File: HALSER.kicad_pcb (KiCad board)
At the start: 4 copper layers, 90.8 x 58.8 mm, 187 parts, among them J1001 RX Sel Header, J1002 RS485 RX Socket, J1003 RS485 TX Socket, J1004 RS-232 Socket, J1005 UART Socket, J301 GPIO, J401 I2C Female Header, J402 I2C Male Header, J501 1-Wire Male Header, J701 CAN Socket, J702 Vin header, J703 CAN Header, J802 USB_C_Receptacle_USB2.0_16P, SW301 SW_Push, SW302 SW_Push, U1001 SN75176BDR, U1002 74LVC2G17, U1003 SP3232EEY-L/TR, U1004 SN75176BDR, U201 SN65HVD230DR, U301 ESP32-C3-MINI-1, U701 LMR54410DBVR, U901 π122U31, U902 XC6206P332MR

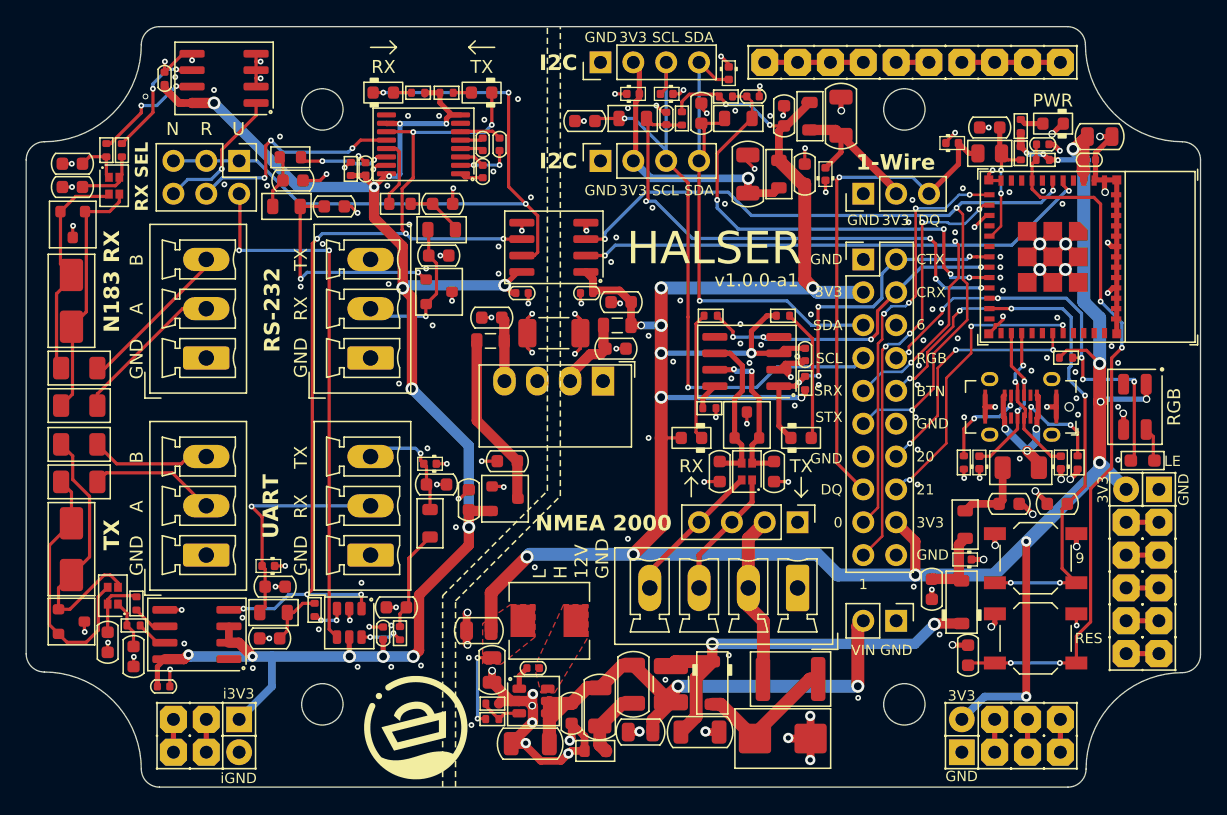
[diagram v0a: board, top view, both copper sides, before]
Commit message: Fix issues found in -a1
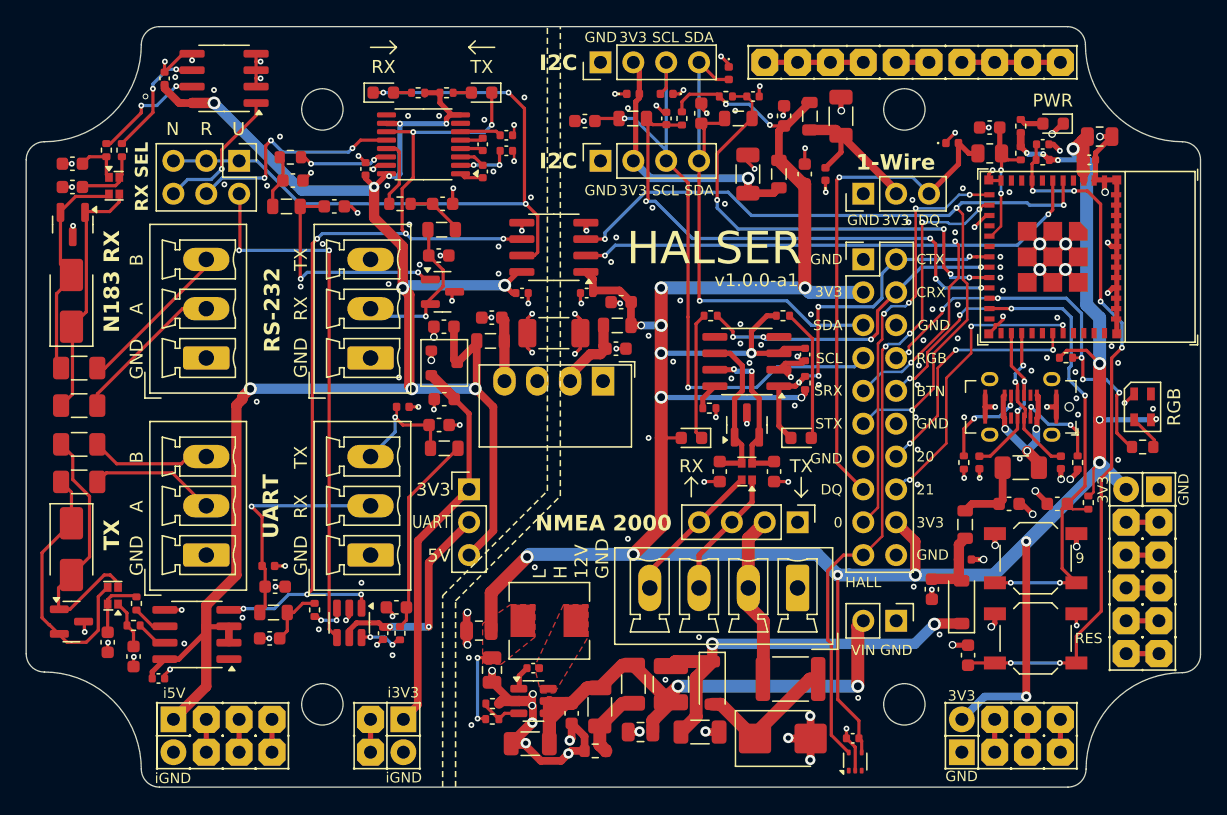
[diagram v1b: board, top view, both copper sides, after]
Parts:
- removed G606: HL-Pictogram, HALSER:HaL_picto_8mm
- removed R901: 330R, PCM_Resistor_SMD_AKL:R_0402_1005Metric
- added C1020: 100nF, Capacitor_SMD:C_0402_1005Metric, F.Cu at (125.7, 85.0)
- added C306: 100nF, Capacitor_SMD:C_0402_1005Metric, F.Cu at (152.5, 131.6)
- added JP1001: UART V-sel, Connector_PinHeader_2.54mm:PinHeader_1x03_P2.54mm_Vertical, F.Cu at (122.8, 112.4)
- added R307: 10k, Resistor_SMD:R_0402_1005Metric, F.Cu at (170.7, 113.4)
- added REF**: ProtoPad_1x01_P2.54_D2.0, HALSER:ProtoPad_1x01_P2.54_D2.0, F.Cu at (117.8, 132.7)
- added REF**: ProtoPad_1x02_P2.54_2.1x2.1_Octagonal, HALSER:ProtoPad_1x02_P2.54_2.1x2.1_Octagonal, F.Cu at (107.6, 132.7)
- added REF**: ProtoPad_1x02_P2.54_2.1x2.1_Octagonal, HALSER:ProtoPad_1x02_P2.54_2.1x2.1_Octagonal, F.Cu at (115.2, 132.7)
- added REF**: ProtoPad_1x01_P2.54_2.0x2.0, HALSER:ProtoPad_1x01_P2.54_2.0x2.0, F.Cu at (117.8, 130.2)
- added U302: KTH1601TL-SF5, Package_TO_SOT_SMD:SOT-553, F.Cu at (152.7, 133.4)
- C1001, C1002, C1003, C1004, C1005, C1006, C1007, C203, C303, C305, C405, C406, C707, C902, C906: footprint PCM_Capacitor_SMD_AKL:C_0402_1005Metric -> Capacitor_SMD:C_0402_1005Metric
- C1008, C1009, C1010, C1011, C1012, C1013, C1014, C1015, C1016, C1017, C1018, C1019, C201, C202, C301, C302, C402, C403, C404, C502, C503, C706, C801, C802, C901, C903, C905, C907, C908: footprint PCM_Capacitor_SMD_AKL:C_0603_1608Metric -> Capacitor_SMD:C_0603_1608Metric
- C304, C702, C708, C709: footprint PCM_Capacitor_SMD_AKL:C_0805_2012Metric -> Capacitor_SMD:C_0805_2012Metric
- C401, C501, C701, C703, C704, C705: footprint PCM_Capacitor_SMD_AKL:C_1206_3216Metric -> Capacitor_SMD:C_1206_3216Metric
- D1001, D1002, D301, D302, D303: footprint PCM_LED_SMD_AKL:LED_0603_1608Metric -> LED_SMD:LED_0603_1608Metric
- D1003, D1004, D1008, D201: footprint PCM_Package_TO_SOT_SMD_AKL:SOT-23 -> Package_TO_SOT_SMD:SOT-23
- D1005, D1006: footprint PCM_Diode_SMD_AKL:D_SMA_TVS -> Diode_SMD:D_SMA
- D1007, D1009, D401, D402, D403, D501, D502, D801, D802, D803: footprint PCM_Diode_SMD_AKL:D_0402_1005Metric -> Diode_SMD:D_0402_1005Metric
- D701, D703: footprint PCM_Diode_SMD_AKL:D_SOD-123 -> Diode_SMD:D_SOD-123
- D702: footprint PCM_Diode_SMD_AKL:D_SMB_TVS -> Diode_SMD:D_SMB
- F1001, F1002, F1003, F1004, F801: footprint PCM_Fuse_AKL:Fuse_1206_3216Metric -> Fuse:Fuse_1206_3216Metric
- F701: footprint PCM_Fuse_AKL:Fuse_1812_4532Metric -> Fuse:Fuse_1812_4532Metric
- FB1001, FB1002, FB1003, FB1004, FB401, FB402, FB403, FB501, FB801: footprint PCM_Ferrite_SMD_AKL:Ferrite_0805_2012Metric -> Inductor_SMD:L_0805_2012Metric
- LED301: value SK68XX-MINI-HS -> SK6805-MICRO-J; footprint PCM_LED_SMD_AKL:LED_SK6812MINI_PLCC4_3.5x3.5mm_P1.75mm -> HALSER:LED_SK6805_PLCC4_2.4x2.7mm_P1.3mm
- R1001, R1002: value 1.5k -> 2.2k; footprint PCM_Resistor_SMD_AKL:R_0402_1005Metric -> Resistor_SMD:R_0402_1005Metric
- R1003, R1004, R1005, R1006, R1007, R1008, R203, R204, R301, R302, R303, R304, R305, R401, R402, R501, R702, R703, R801, R802: footprint PCM_Resistor_SMD_AKL:R_0402_1005Metric -> Resistor_SMD:R_0402_1005Metric
- R1009, R1010, R701: footprint PCM_Resistor_SMD_AKL:R_0603_1608Metric -> Resistor_SMD:R_0603_1608Metric
- R306: value 0R -> 470R; footprint PCM_Resistor_SMD_AKL:R_0603_1608Metric_Pad0.98x0.95mm_HandSolder -> Resistor_SMD:R_0603_1608Metric
- R502: footprint PCM_Resistor_SMD_AKL:R_0805_2012Metric -> Resistor_SMD:R_0805_2012Metric
- U1001, U1004, U201, U901: footprint PCM_Package_SO_AKL:SOIC-8_3.9x4.9mm_P1.27mm -> Package_SO:SOIC-8_3.9x4.9mm_P1.27mm
- U1002, U701: footprint PCM_Package_TO_SOT_SMD_AKL:SOT-23-6 -> Package_TO_SOT_SMD:SOT-23-6
- U1003: footprint PCM_Package_SO_AKL:TSSOP-16_4.4x5mm_P0.65mm -> Package_SO:TSSOP-16_4.4x5mm_P0.65mm
- moved G602 13.7 mm to (133.0, 128.9)
- moved G603 13.7 mm to (145.6, 129.3)
- moved U902 11.5 mm to (120.9, 102.6)
- moved C907 11.5 mm to (120.9, 99.8)
- moved C908 8.02 mm to (120.9, 105.4), turned to 180 degrees
- moved FB1001 5.90 mm to (120.9, 109.2), turned to 180 degrees
- moved REF** 5.08 mm to (100.0, 132.7)
- moved REF** 5.08 mm to (100.0, 130.2)
- moved REF** 5.08 mm to (105.1, 132.7)
- moved D1007 4.88 mm to (117.7, 106.0)
- moved C1014 4.60 mm to (120.5, 107.4)
- moved R306 1.05 mm to (174.9, 109.1)
- moved C1002 0.74 mm to (98.8, 127.0)
- moved C1007 0.72 mm to (125.7, 86.2), turned to 180 degrees
- moved LED301 0.59 mm to (174.9, 106.0), turned to -90 degrees
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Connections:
- C1001 pad 1: GND1 -> GND_ISO
- C1001 pad 2: +3.3V_1 -> +5V_ISO
- C1002 pad 1: GND1 -> GND_ISO
- C1002 pad 2: +3.3V_1 -> +5V_ISO
- C1003 pad 1: GND1 -> GND_ISO
- C1003 pad 2: +3.3V_1 -> +5V_ISO
- C1005 pad 1: GND1 -> /Serial interfaces/Vsel
- C1005 pad 2: +3.3V_1 -> GND_ISO
- C1007 pad 1: Net-(U1003-VS+) -> GND_ISO
- C1007 pad 2: Net-(U1003-VS-) -> Net-(U1003-VS+)
- C1008 pad 2: GND1 -> GND_ISO
- C1009 pad 2: GND1 -> GND_ISO
- C1010 pad 2: GND1 -> GND_ISO
- C1011 pad 2: GND1 -> GND_ISO
- C1012 pad 2: GND1 -> GND_ISO
- C1013 pad 2: GND1 -> GND_ISO
- C1014 pad 2: GND1 -> GND_ISO
- C1015 pad 2: GND1 -> GND_ISO
- C1016 pad 2: GND1 -> GND_ISO
- C1017 pad 2: GND1 -> GND_ISO
- C1018 pad 2: GND1 -> GND_ISO
- C1019 pad 2: GND1 -> GND_ISO
- C904 pad 2: GND1 -> GND_ISO
- C905 pad 2: GND1 -> GND_ISO
- C906 pad 1: +3.3V_1 -> +5V_ISO
- C906 pad 2: GND1 -> GND_ISO
- C907 pad 1: /Isolation barrier/5V_unreg -> +5V_ISO
- C907 pad 2: GND1 -> GND_ISO
- C908 pad 1: +3.3V_1 -> +3.3V_ISO
- C908 pad 2: GND1 -> GND_ISO
- D1003 pad 3: GND1 -> GND_ISO
- D1004 pad 3: GND1 -> GND_ISO
- D1007 pad 1: GND1 -> GND_ISO
- D1008 pad 3: GND1 -> GND_ISO
- D1009 pad 1: GND1 -> GND_ISO
- J1002 pad 1: GND1 -> GND_ISO
- J1003 pad 1: GND1 -> GND_ISO
- J1004 pad 1: GND1 -> GND_ISO
- J1005 pad 1: GND1 -> GND_ISO
- L902 pad 2: /Isolation barrier/5V_unreg -> +5V_ISO
- PS901 pad 3: GND1 -> GND_ISO
- R1001 pad 1: +3.3V_1 -> +5V_ISO
- R1002 pad 1: +3.3V_1 -> +5V_ISO
- REF** pad 1: GND1 -> GND_ISO
- REF** pad 1: +3.3V_1 -> +5V_ISO
- U1001 pad 2: GND1 -> GND_ISO
- U1001 pad 3: GND1 -> GND_ISO
- U1001 pad 4: GND1 -> GND_ISO
- U1001 pad 5: GND1 -> GND_ISO
- U1001 pad 8: +3.3V_1 -> +5V_ISO
- U1002 pad 2: GND1 -> GND_ISO
- U1002 pad 5: +3.3V_1 -> /Serial interfaces/Vsel
- U1003 pad 10: +3.3V_1 -> +5V_ISO
- U1003 pad 15: GND1 -> GND_ISO
- U1003 pad 16: +3.3V_1 -> +5V_ISO
- U1003 pad 8: +3.3V_1 -> +5V_ISO
- U1004 pad 2: +3.3V_1 -> +5V_ISO
- U1004 pad 3: +3.3V_1 -> +5V_ISO
- U1004 pad 5: GND1 -> GND_ISO
- U1004 pad 8: +3.3V_1 -> +5V_ISO
- U301 pad 5: /SER_RX -> /SER_TX
- U301 pad 6: /SER_TX -> /SER_RX
- U901 pad 5: GND1 -> GND_ISO
- U901 pad 8: +3.3V_1 -> +5V_ISO
- U902 pad 1: GND1 -> GND_ISO
- U902 pad 2: +3.3V_1 -> +3.3V_ISO
- U902 pad 3: /Isolation barrier/5V_unreg -> +5V_ISO
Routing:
- net +5V_ISO: track 0.00 -> 142.9 mm, vias 0 -> 10
- net +3.3V_1: track 127.4 -> 0.00 mm, vias 14 -> 0
- net GND1: track 38.3 -> 0.00 mm, vias 69 -> 0
- net GND_ISO: track 0.00 -> 36.7 mm, vias 0 -> 64
- net +3.3V_ISO: track 0.00 -> 29.9 mm
- net /ESP32/GPIO1: track 34.0 -> 52.0 mm
- net +3.3V: track 235.4 -> 252.6 mm, vias 25 -> 26
- net /Serial interfaces/Vsel: track 0.00 -> 16.4 mm, vias 0 -> 2
- net /Isolation barrier/5V_unreg: track 13.5 -> 0.00 mm
- net Net-(C1012-Pad1): track 7.89 -> 15.6 mm
- net GND: track 129.2 -> 132.5 mm, vias 130 -> 129
- net /ESP32/GPIO8: track 34.0 -> 31.6 mm
- net /SER_TX: track 62.2 -> 63.9 mm
- net /ESP32/GPIO9: track 47.8 -> 49.4 mm
- net /SER_RX: track 56.0 -> 55.5 mm
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- added copper zone on In1.Cu, net GND_ISO
- added copper zone on In2.Cu, net GND_ISO
- removed copper zone on In1.Cu, net GND1
- removed copper zone on In2.Cu, net GND1
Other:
- board text added: "5V"
- board text added: "HALL"
- board text added: "i5V"
- board text removed: "1"
- board text removed: "6"
- board text removed: "LE"

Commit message: Bump versions
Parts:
- added G606: HL-Pictogram, HALSER:HaL_picto_8mm, F.Cu at (129.2, 112.8)
- R1009: renamed from R1003; footprint Resistor_SMD:R_0402_1005Metric -> Resistor_SMD:R_0603_1608Metric
- R1010: renamed from R1004; footprint Resistor_SMD:R_0402_1005Metric -> Resistor_SMD:R_0603_1608Metric
- moved U1002 43.1 mm to (101.7, 123.6)
- moved U1004 43.1 mm to (103.9, 80.6)
- moved R1003 40.6 mm to (96.6, 126.7), turned to 180 degrees
- moved R1004 39.5 mm to (96.6, 125.6), turned to 180 degrees
- moved C1009 36.3 mm to (95.0, 123.4), turned to -90 degrees
- moved C1016 36.1 mm to (92.2, 88.2), turned to 180 degrees
- moved C1010 35.7 mm to (92.2, 89.9), turned to 180 degrees
- moved C1015 34.7 mm to (96.8, 123.4), turned to -90 degrees
- moved R1005 33.2 mm to (95.2, 89.7)
- moved R1006 32.8 mm to (95.2, 88.5), turned to 180 degrees
- moved FL1001 31.7 mm to (95.8, 120.6), turned to -90 degrees
- moved FL1002 28.1 mm to (95.3, 92.5), turned to 0 degrees
- moved D1003 23.0 mm to (92.2, 114.9)
- moved D1004 22.6 mm to (92.4, 100.0)
- moved D1007 22.6 mm to (92.2, 120.4)
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- renumbered C1020 to C1007, C1007 to C1008, C1008 to C1009, C1009 to C1010, C1012 to C1011, C1013 to C1012, C1016 to C1013, C1017 to C1014, C1010 to C1015, C1011 to C1016, C1014 to C1017, C1015 to C1018, C1018 to C1019, C1019 to C1020, C303 to C301, C304 to C302, C305 to C303, C306 to C304, C301 to C305, C302 to C306, D1008 to D1005, D1007 to D1006, D1005 to D1007, D1006 to D1008, J402 to J401, J401 to J402, J703 to J701, J701 to J702, J702 to J703, J802 to J801, R1005 to R1003, R1006 to R1004, R1007 to R1005, R1008 to R1006, R1009 to R1007, R1010 to R1008, R203 to R201, R204 to R202, R306 to R301, R307 to R302, R301 to R303, R302 to R304, R303 to R305, R304 to R306, R305 to R307, U1002 to U1001, U1001 to U1002
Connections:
- net /Power input/VIN renamed /Power input/VIN_BUCK
- C1011 pad 1: Net-(C1012-Pad1) -> /Serial interfaces/UART_TX_OUT
- C1012 pad 1: Net-(C1013-Pad1) -> /Serial interfaces/UART_RX_IN
- C1013 pad 1: Net-(C1016-Pad1) (its old number) -> /Serial interfaces/RS232_TX_OUT
- C1014 pad 1: Net-(C1017-Pad1) -> /Serial interfaces/RS232_RX_IN
- C1017 pad 1: /Serial interfaces/UART_TX_C -> Net-(D1006-A2)
- C1018 pad 1: /Serial interfaces/UART_RX_C -> Net-(D1009-A2)
- C1019 pad 1: /Serial interfaces/RS232_TX_C -> Net-(D1005-A1)
- C1020 pad 1: /Serial interfaces/RS232_RX_C -> Net-(D1005-A2)
- D1003 pad 1: /Serial interfaces/RS485_RX_A_C -> Net-(D1003-A1)
- D1003 pad 2: /Serial interfaces/RS485_RX_B_C -> Net-(D1003-A2)
- D1005 pad 1: /Serial interfaces/RS232_TX_C -> Net-(D1005-A1)
- D1005 pad 2: /Serial interfaces/RS232_RX_C -> Net-(D1005-A2)
- D1006 pad 2: /Serial interfaces/UART_TX_C -> Net-(D1006-A2)
- D1007 pad 1: /Serial interfaces/RS485_RX_A_C -> Net-(D1003-A2)
- D1007 pad 2: /Serial interfaces/RS485_RX_B_C -> Net-(D1003-A1)
- D1009 pad 2: /Serial interfaces/UART_RX_C -> Net-(D1009-A2)
- F1001 pad 1: Net-(J1002-Pin_3) -> /Serial interfaces/RS485_RX_B_C
- F1001 pad 2: /Serial interfaces/RS485_RX_B_C -> Net-(D1003-A1)
- F1002 pad 1: Net-(J1002-Pin_2) -> /Serial interfaces/RS485_RX_A_C
- F1002 pad 2: /Serial interfaces/RS485_RX_A_C -> Net-(D1003-A2)
- FB1001 pad 1: Net-(C1012-Pad1) -> /Serial interfaces/UART_TX_OUT
- FB1001 pad 2: /Serial interfaces/UART_TX_C -> Net-(D1006-A2)
- FB1002 pad 1: Net-(C1013-Pad1) -> /Serial interfaces/UART_RX_IN
- FB1002 pad 2: /Serial interfaces/UART_RX_C -> Net-(D1009-A2)
- FB1003 pad 1: Net-(C1016-Pad1) (its old number) -> /Serial interfaces/RS232_TX_OUT
- FB1003 pad 2: /Serial interfaces/RS232_TX_C -> Net-(D1005-A1)
- FB1004 pad 1: Net-(C1017-Pad1) -> /Serial interfaces/RS232_RX_IN
- FB1004 pad 2: /Serial interfaces/RS232_RX_C -> Net-(D1005-A2)
- FL1001 pad 2: /Serial interfaces/RS485_RX_B_C -> Net-(D1003-A1)
- FL1001 pad 3: /Serial interfaces/RS485_RX_A_C -> Net-(D1003-A2)
- J1002 pad 2: Net-(J1002-Pin_2) -> /Serial interfaces/RS485_RX_A_C
- J1002 pad 3: Net-(J1002-Pin_3) -> /Serial interfaces/RS485_RX_B_C
- R1007 pad 1: /Serial interfaces/RS232_TX_OUT -> Net-(D1005-A1)
- R1007 pad 2: Net-(C1016-Pad1) (its old number) -> /Serial interfaces/RS232_TX_C
- R1008 pad 1: /Serial interfaces/RS232_RX_IN -> Net-(D1005-A2)
- R1008 pad 2: Net-(C1017-Pad1) -> /Serial interfaces/RS232_RX_C
- R1009 pad 1: /Serial interfaces/UART_TX_OUT -> Net-(D1006-A2)
- R1009 pad 2: Net-(C1012-Pad1) -> /Serial interfaces/UART_TX_C
- R1010 pad 1: /Serial interfaces/UART_RX_IN -> Net-(D1009-A2)
- R1010 pad 2: Net-(C1013-Pad1) -> /Serial interfaces/UART_RX_C
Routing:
- net /Serial interfaces/RS485_RX: track 11.3 -> 37.7 mm
- net /Serial interfaces/UART_TX_OUT: track 3.38 -> 19.8 mm
- net Net-(C1012-Pad1): track 15.6 -> 0.00 mm
- net Net-(D1003-A2): track 0.00 -> 15.3 mm
- net Net-(D1005-A1): track 0.00 -> 14.0 mm, vias 0 -> 2
- net Net-(D1006-A2): track 0.00 -> 13.2 mm, vias 0 -> 2
- net /Serial interfaces/RS232_RX_IN: track 5.44 -> 18.0 mm, vias 0 -> 4
- net Net-(J1002-Pin_3): track 12.2 -> 0.00 mm
- net Net-(D1003-A1): track 0.00 -> 12.1 mm
- net Net-(J1002-Pin_2): track 12.1 -> 0.00 mm
- net /Serial interfaces/RS485_TX_B: track 2.47 -> 12.0 mm
- net /Isolation barrier/iVOB: track 75.0 -> 84.5 mm, vias 8 -> 9
- net /Serial interfaces/RS485_TX_A: track 2.72 -> 11.9 mm
- net /Serial interfaces/RS232_TX_C: track 17.6 -> 8.86 mm
- net Net-(D1004-A2): track 21.0 -> 12.8 mm
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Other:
- board text added: "UART TX"
- board text added: "v1.0.0"
- board text removed: "v1.0.0-a1"
